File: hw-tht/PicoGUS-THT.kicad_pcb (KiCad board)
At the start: 2 copper layers, 103.7 x 99.8 mm, 77 parts, among them J1 IRQDMA_JP, J3 Bus_ISA_8bit, J5 SJ1-3535NG, J6 UART_TX, J7 USB power jumper, J8 SJ1-3535NG-GR, J9 Waveblaster, U1 Pico, U10 74AHCT126, U11 NE5532, U2 74AHC244, U3 SN74CB3T3257, U4 SN74CB3T3257, U5 74AHC14, U6 74AHC00, U7 74AHC00, U8 APS6404L-3SQR-SN, U9 PCM5100A

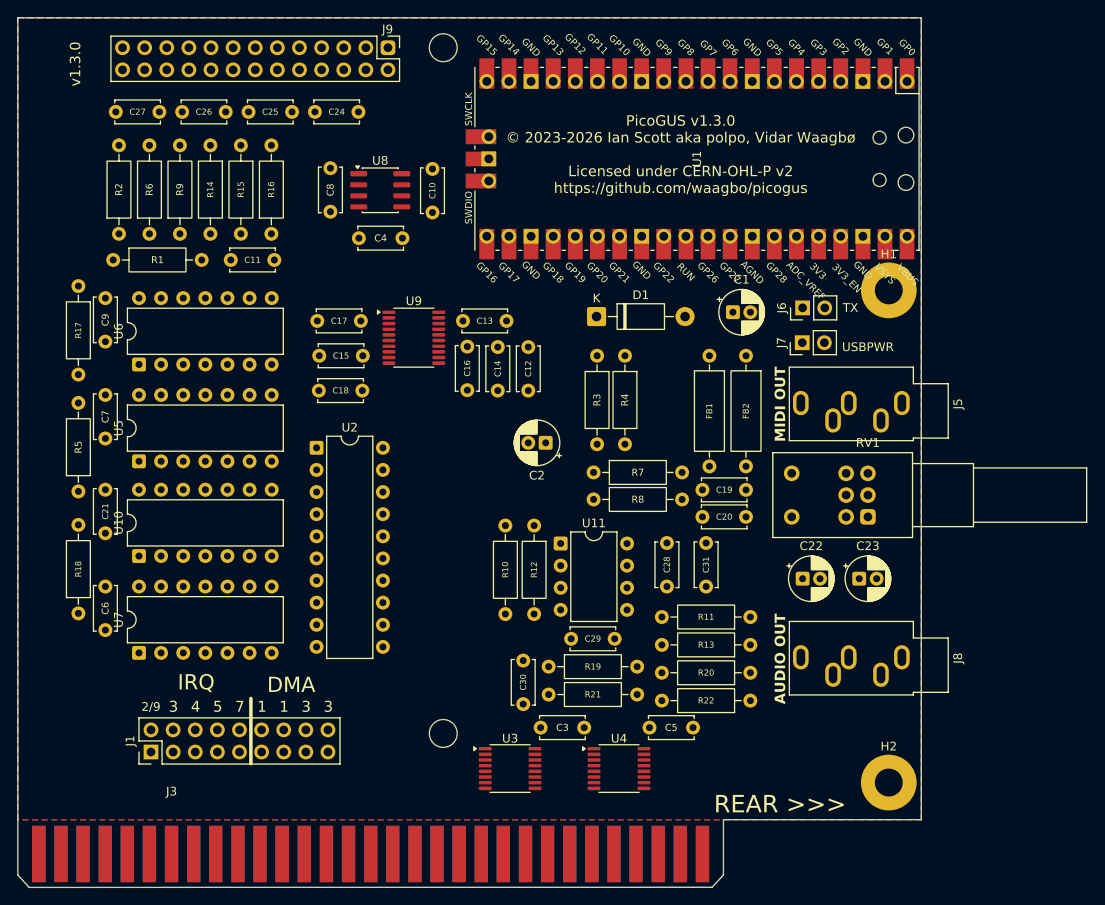
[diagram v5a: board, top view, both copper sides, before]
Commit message: hw-tht: route the through-hole board, silkscreen pass
- Fully routed (Freerouting 1.9.0 with GND routed as a net, pours filled
  afterwards): 0 DRC errors, every net connected. Hand pre-routes for
  the DAC: GND pins 16/19 to a via under the chip, VNEG to C17.
- GND pour on both layers with stitching vias.
- Silkscreen: DIP labels inside the outlines, colliding labels moved,
  DAC / MIXER / WT VOL / WAVEBLASTER legends, one-arrow REAR labels
  centred on the H2 screw hole. Back: info text in the Pico area; credit
  list, pig, Colorado flag and JLC placeholder removed.

Remaining DRC warnings are cosmetic: small label text, a few pads with
fewer thermal spokes, silk near the board edge.

Co-Authored-By: Claude Opus 5.5 <noreply@anthropic.com>
Claude-Session: https://claude.ai/code/session_011utN3x8yYUNDvkpGCEq5yD
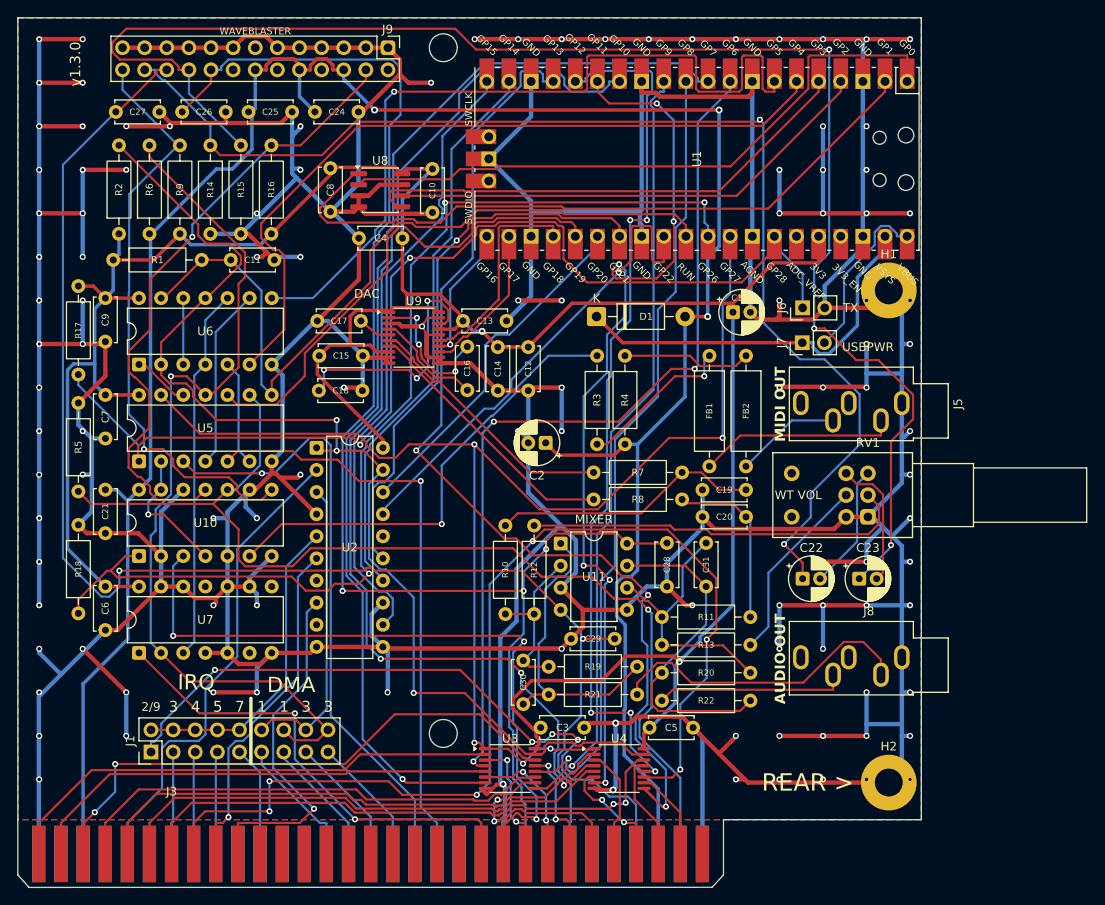
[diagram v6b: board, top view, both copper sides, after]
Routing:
- net GND: track 0.00 -> 1153.9 mm, vias 0 -> 112
- net +3V3: track 0.00 -> 308.9 mm, vias 0 -> 2
- net +5V: track 0.00 -> 274.1 mm, vias 0 -> 3
- net /Wavetable & line out/WT_R: track 0.00 -> 177.0 mm, vias 0 -> 3
- net +12V: track 0.00 -> 165.9 mm, vias 0 -> 3
- net -12V: track 0.00 -> 159.9 mm, vias 0 -> 2
- net ADS: track 0.00 -> 148.7 mm, vias 0 -> 5
- net /Wavetable & line out/WT_L: track 0.00 -> 141.5 mm, vias 0 -> 2
- net ~{BUSOE}: track 0.00 -> 132.4 mm, vias 0 -> 3
- net AD4: track 0.00 -> 130.2 mm, vias 0 -> 3
- net AD1: track 0.00 -> 127.8 mm, vias 0 -> 1
- net UART_TX: track 0.00 -> 126.3 mm, vias 0 -> 2
- net A7: track 0.00 -> 124.7 mm, vias 0 -> 6
- net ~{RI/OCHRDY}: track 0.00 -> 123.1 mm, vias 0 -> 3
- net RESET: track 0.00 -> 121.3 mm, vias 0 -> 1
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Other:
- board text added: "< REAR"
- board text added: "DAC"
- board text added: "MIXER"
- board text added: "PicoGUS v1.3.0 © 2023-2026 Ian Scott (polpo), Vidar Waagbø (waagbo) Licensed under CERN-OHL-P v2 https://github.com/waagbo/picogus Thanks to all the people that have contributed over the years!"
- board text added: "REAR >"
- board text added: "WAVEBLASTER"
- board text added: "WT VOL"
- board text removed: "JLCJLCJLCJLC"
- board text removed: "Leaded Solder Nicole Express PickledDog rasz_pl root42 Studio8502 SuperIlu TechAmbrosia Todd Gill tom7 Tube Time vswitchzero yyzkevin Zago everyone on Mastodon and Vogons everyone who contributed hardware or $$$ and the Retro Pico Hardware Discord for various combinations of inspiration, ideas, code, and/or help"
- board text removed: "PicoGUS v1.3.0 © 2023-2026 Ian Scott aka polpo, Vidar Waagbø Licensed under CERN-OHL-P v2 https://github.com/waagbo/picogus"
- board text removed: "REAR >>>"
- board text removed: "REAR OF <<< PC"
- board text removed: "designed in Colorado"
- board text removed: "thanks to: 48kRAM Aaron Giles Adrian Black Chrissy Claude Schwarz deck/scoopex djh0ffman FireTwoOneNine foone FreddyV furan Graham Sanderson HeathenUK indigoparadox Jim Leonard Jonathan Campbell Konrad Beckmann"

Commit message: hw-tht: cleaner audio supplies, bipolar WT coupling caps, circuit-block groups
- DAC AVDD (U9 pin 8) gets its own rail behind ferrite bead FB3, with C13/C15
  at the pin; DVDD/CPVDD stay on the Pico 3V3.
- NE5532 +/-12 V from ISA through R23/R24 (10R) + C32/C33 (47uF) RC filters,
  C28/C29 0.1uF stay at the op-amp pins.
- C22/C23 WT coupling caps are now 10uF bipolar (Panasonic ECE-A1HN100U):
  the DC across them depends on the daughterboard.
- Every chip and its decoupling caps/resistors form a KiCad group.
- DAC pre-routes reworked (VNEG via B.Cu, XSMT via); RUN RC moved out of the
  Pico fan-in. Fully routed, 0 DRC errors, 0 unconnected.
- BOM: new lines for R23/R24, FB3, C32/C33; README has DigiKey cost in NOK.

Co-Authored-By: Claude Opus 5.5 <noreply@anthropic.com>
Claude-Session: https://claude.ai/code/session_011utN3x8yYUNDvkpGCEq5yD
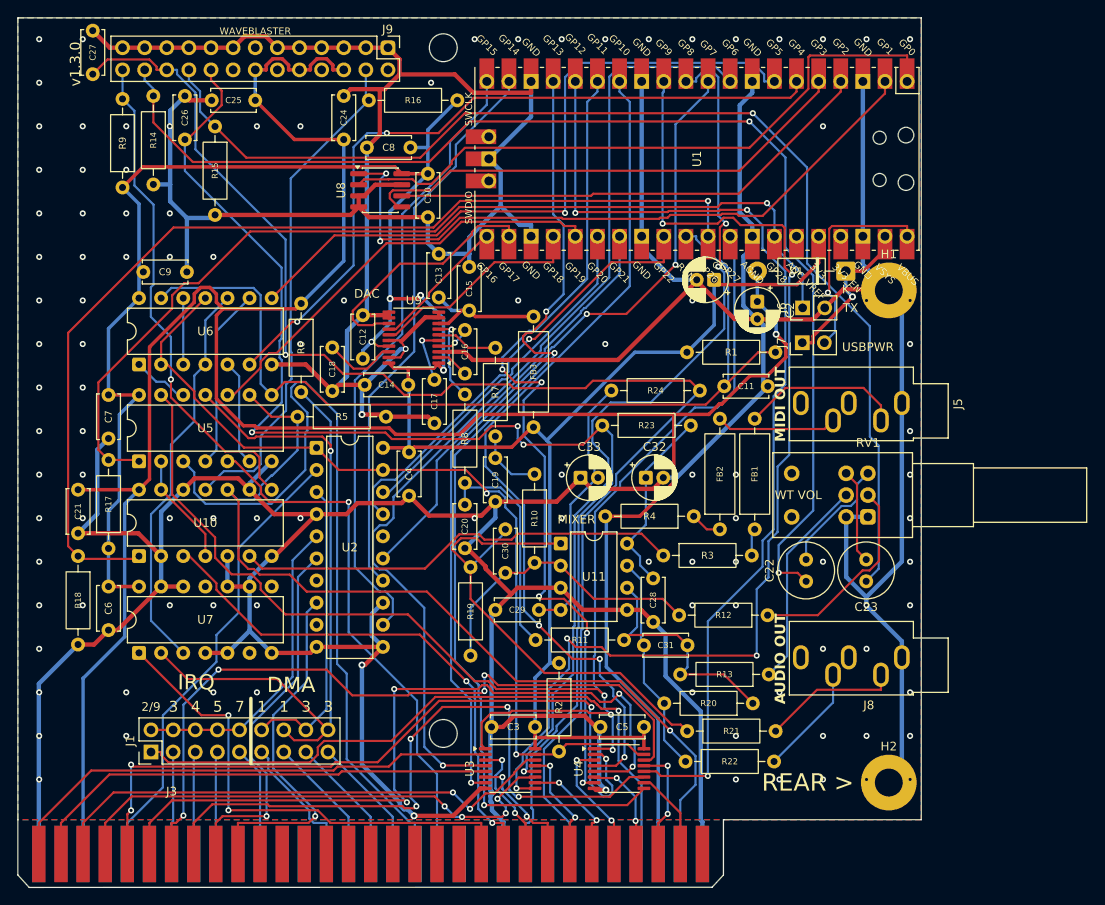
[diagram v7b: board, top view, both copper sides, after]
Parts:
- added C32: 47uF, Capacitor_THT:CP_Radial_D5.0mm_P2.00mm, F.Cu at (188.5, 89.0)
- added C33: 47uF, Capacitor_THT:CP_Radial_D5.0mm_P2.00mm, F.Cu at (181.0, 89.0)
- added FB3: Ferrite bead, Resistor_THT:R_Axial_DIN0309_L9.0mm_D3.2mm_P12.70mm_Horizontal, F.Cu at (175.6, 83.2)
- added R23: 10, Resistor_THT:R_Axial_DIN0207_L6.3mm_D2.5mm_P10.16mm_Horizontal, F.Cu at (183.5, 83.0)
- added R24: 10, Resistor_THT:R_Axial_DIN0207_L6.3mm_D2.5mm_P10.16mm_Horizontal, F.Cu at (194.7, 79.0)
- C22, C23: value 10uF -> 10uF bipolar; footprint Capacitor_THT:CP_Radial_D5.0mm_P2.00mm -> Capacitor_THT:C_Radial_D6.3mm_H11.0mm_P2.50mm
- moved R2 70.6 mm to (178.5, 110.3), turned to -90 degrees
- moved R1 66.7 mm to (193.2, 74.6)
- moved C11 58.5 mm to (197.5, 78.5)
- moved R17 30.3 mm to (126.8, 97.1), turned to 90 degrees
- moved C2 29.2 mm to (201.3, 68.8), turned to -90 degrees
- moved D1 29.1 mm to (211.5, 65.3), turned to 180 degrees
- moved R12 28.7 mm to (202.5, 104.8), turned to 180 degrees
- moved C20 27.5 mm to (167.7, 97.1), turned to 90 degrees
- moved R5 26.6 mm to (148.5, 82.0), turned to 0 degrees
- moved R16 26.3 mm to (166.8, 45.7), turned to 180 degrees
- moved R11 24.8 mm to (175.8, 107.6), turned to 0 degrees
- moved C4 24.6 mm to (161.3, 86.1), turned to -90 degrees
- moved R3 24.2 mm to (190.5, 97.9), turned to 0 degrees
- moved C19 23.8 mm to (171.2, 91.8), turned to 90 degrees
- moved C12 20.9 mm to (156.0, 70.3), turned to -90 degrees
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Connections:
- C13 pad 2: +3V3 -> /PCM5100 audio/AVDD
- C15 pad 1: +3V3 -> /PCM5100 audio/AVDD
- C28 pad 1: +12V -> /Wavetable & line out/+12VA
- C29 pad 2: -12V -> /Wavetable & line out/-12VA
- U11 pad 4: -12V -> /Wavetable & line out/-12VA
- U11 pad 8: +12V -> /Wavetable & line out/+12VA
- U9 pad 8: +3V3 -> /PCM5100 audio/AVDD
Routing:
- net GND: track 1153.9 -> 830.6 mm, vias 112 -> 109
- net A7: track 124.7 -> 77.3 mm, vias 6 -> 4
- net /Wavetable & line out/WT_R: track 177.0 -> 133.4 mm, vias 3 -> 1
- net AD3: track 88.8 -> 126.9 mm, vias 1 -> 5
- net AD4: track 130.2 -> 97.3 mm
- net /Wavetable & line out/-12VA: track 0.00 -> 31.1 mm
- net A5: track 58.4 -> 89.0 mm, vias 0 -> 4
- net ~{BUSOE}: track 132.4 -> 102.0 mm, vias 3 -> 2
- net AD1: track 127.8 -> 98.1 mm, vias 1 -> 3
- net +3V3: track 308.9 -> 281.2 mm, vias 2 -> 4
- net /VSYS: track 44.9 -> 18.7 mm, vias 0 -> 1
- net /PCM5100 audio/AUDIO_L: track 31.0 -> 7.77 mm
- net Net-(U9-OUTL): track 30.0 -> 7.12 mm
- net A4: track 62.0 -> 84.8 mm, vias 0 -> 4
- net Net-(C30-Pad2): track 35.1 -> 57.2 mm
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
